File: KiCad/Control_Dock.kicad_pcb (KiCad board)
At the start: 2 copper layers, 101.6 x 68 mm, 21 parts, among them J1 Barrel_Jack, SW2 SW_Push, SW3 SW_Push, SW4 SW_Push

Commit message: worked on PCB
still not finished :(
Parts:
- removed J1: Barrel_Jack, DLS_custom_footprints:Push_button pads
- added BT1: 12V Li-ion, DLS_custom_footprints:Push_button pads, F.Cu at (53.3, 121.9)
- added SW1: SW_Nidec_CAS-120A1, custom:3-pin switch, F.Cu at (55.9, 114.3)
- ROT1: footprint DLS_custom_footprints:Alps EC11E series encoders -> Rotary_Encoder:RotaryEncoder_Alps_EC11E-Switch_Vertical_H20mm_MountingHoles
- moved SW2 18.1 mm to (103.0, 70.0)
- moved SW3 18.1 mm to (103.1, 79.1)
- moved SW4 18.1 mm to (103.1, 88.1)
- moved ROT1 3.94 mm to (170.3, 100.9), turned to 90 degrees
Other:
- board size 101.6 x 68 mm -> 137.9 x 68 mm

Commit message: Control PCB ready for review
Ready for review, then send to manufacturer
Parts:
- added Down Right: MountingHole_2.2mm_M2, MountingHole:MountingHole_2.2mm_M2, F.Cu at (180.0, 128.7)
- added UP Left: MountingHole_2.2mm_M2, MountingHole:MountingHole_2.2mm_M2, F.Cu at (50.9, 53.0)
- moved SW4 71.7 mm to (167.6, 119.4), turned to 0 degrees
- moved SW3 67.6 mm to (157.5, 119.4), turned to 0 degrees
- moved SW2 66.3 mm to (147.3, 119.4), turned to 0 degrees
- moved Processor1 57.2 mm to (139.7, 71.1), turned to 90 degrees
- moved R6 56.6 mm to (157.2, 77.5)
- moved C3 52.7 mm to (163.0, 77.5)
- moved D3 47.5 mm to (170.2, 109.2), turned to 90 degrees
- moved R4 42.6 mm to (148.0, 94.1), turned to -90 degrees
- moved SW1 41.2 mm to (49.8, 73.6), turned to 90 degrees
- moved D2 35.4 mm to (157.3, 109.1), turned to 90 degrees
- moved R5 35.0 mm to (166.9, 94.0), turned to -90 degrees
- moved R1 33.7 mm to (141.7, 113.4), turned to 180 degrees
- moved R7 32.6 mm to (149.9, 124.6), turned to -90 degrees
- moved C2 31.2 mm to (148.0, 97.7), turned to -90 degrees
- moved D1 30.0 mm to (144.9, 108.8), turned to 90 degrees
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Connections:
- BT1 pad 2: Net-(BT1--) -> GND
- SW1 pad 3: Net-(BT1--) -> GND
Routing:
- net +3.3V: track 0.00 -> 166.4 mm
- net /a3: track 0.00 -> 113.7 mm, vias 0 -> 1
- net +12V: track 0.00 -> 110.4 mm
- net /a2: track 0.00 -> 104.5 mm, vias 0 -> 1
- net /a1: track 0.00 -> 95.9 mm, vias 0 -> 1
- net /L2: track 0.00 -> 65.8 mm
- net /L3: track 0.00 -> 61.0 mm
- net /L1: track 0.00 -> 57.8 mm
- net Net-(BT1-+): track 0.00 -> 51.0 mm
- net ROT1_A: track 0.00 -> 49.9 mm, vias 0 -> 1
- net ROT1_B: track 0.00 -> 40.5 mm, vias 0 -> 1
- net ROT1_Sw: track 0.00 -> 31.2 mm, vias 0 -> 3
- net Net-(D3-K): track 0.00 -> 5.52 mm
- net Net-(D1-K): track 0.00 -> 5.49 mm
- net Net-(D2-K): track 0.00 -> 5.46 mm
- added copper zone on B.Cu, net GND
- added copper zone on F.Cu, net GND
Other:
- board size 137.9 x 68 mm -> 135 x 81.6 mm
- board text added: "${PROJECTNAME}, V${REVISION}"
- board text added: "Battery"
- board text added: "Dedicated to Hadwa <3, my beloved"
- board text added: "GND"

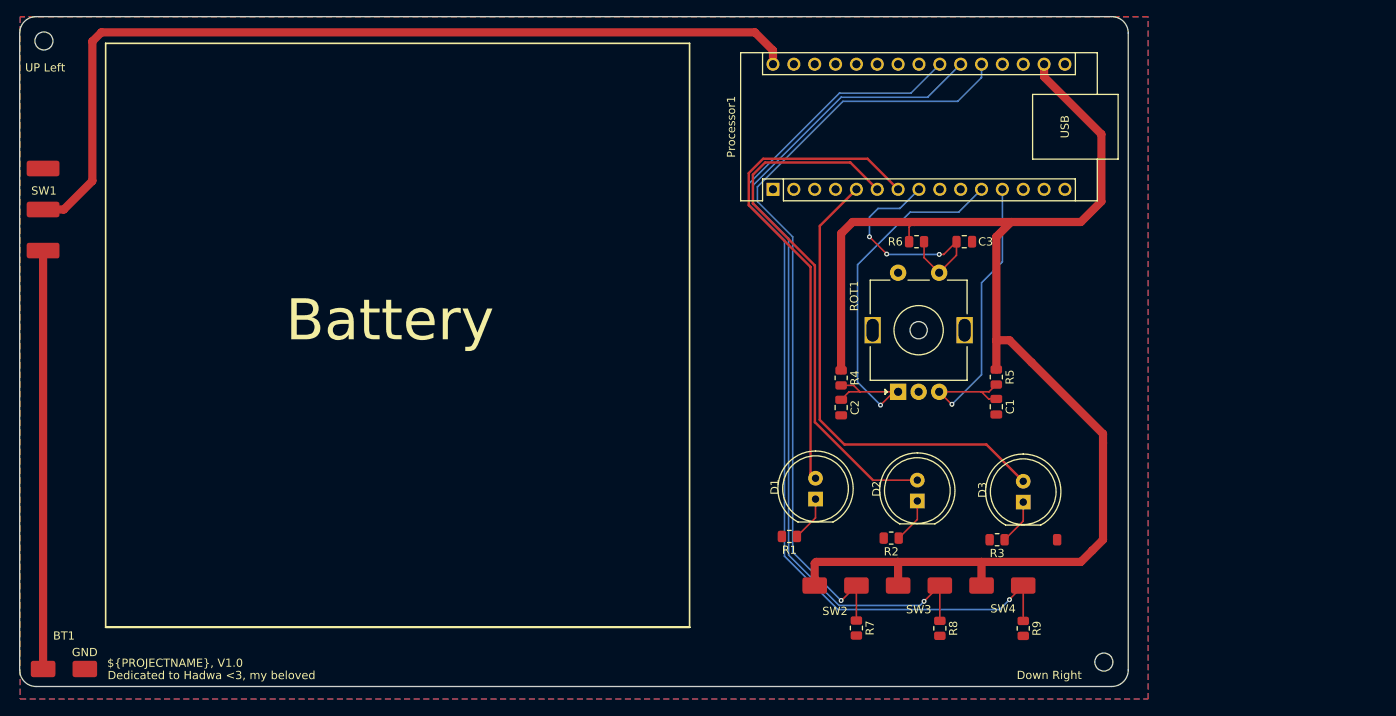
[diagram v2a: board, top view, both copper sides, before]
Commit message: Finished Control PCB desing
Sent JLCPCB for manufacturing
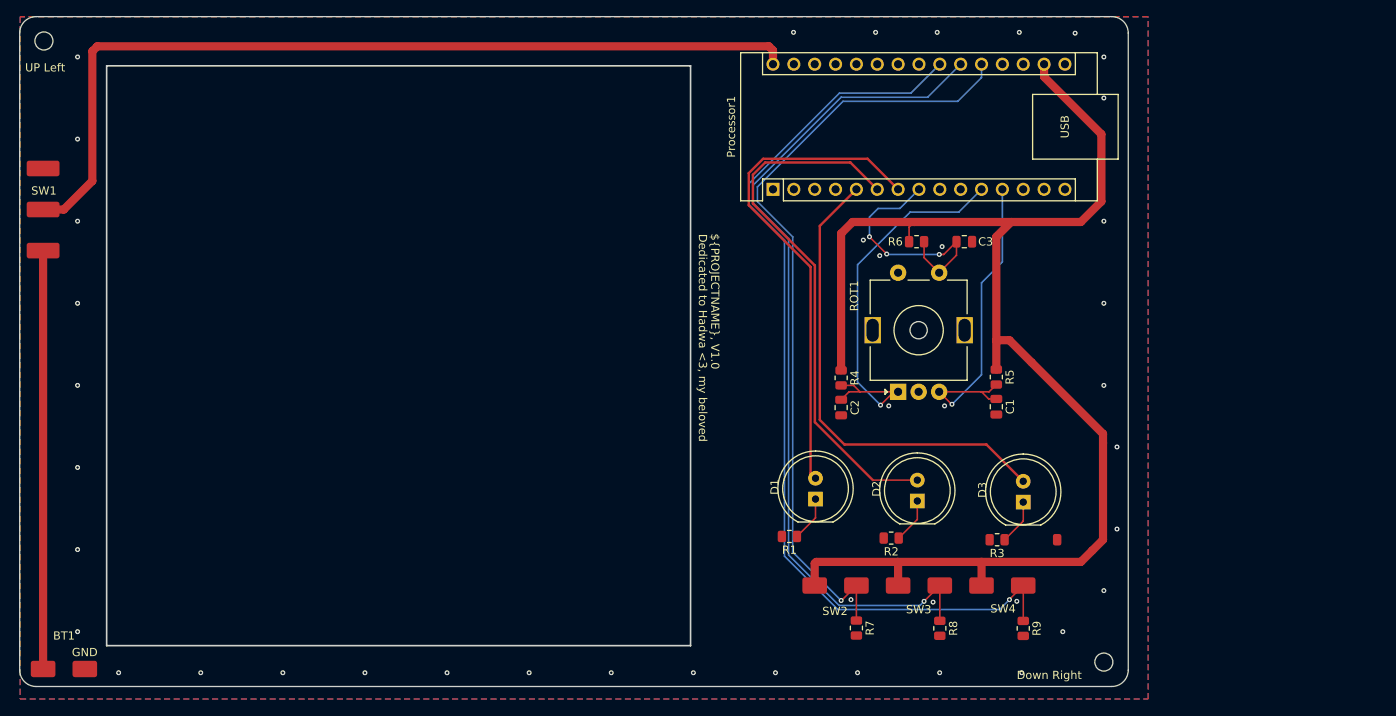
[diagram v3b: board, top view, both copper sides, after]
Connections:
- ROT1 pad 2: (no net) -> GND
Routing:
- net +12V: track 110.4 -> 108.3 mm
- net GND: vias 0 -> 42
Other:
- outline, holes or cut-outs redrawn
- board text removed: "Battery"
